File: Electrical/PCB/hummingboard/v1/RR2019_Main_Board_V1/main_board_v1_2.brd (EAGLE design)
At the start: 100 x 75 mm, 129 parts, among them CN1 MIRCO_B, J1 JTAG_SWD, J10 I2C_5V_4, J11 SERVO_LEFT, J12 SERVO_RIGHT, J13 ESC, J14 5V_INPUT, J15 QUAD_ENCODER_2, J17 I2C_5V_FXIO_1, J18 I2C_5V_FXIO_2, J2 REAR_ENCODER, J20 QUAD_ENCODER_1, J21 BLDC_HALL, J22 SPI_FXIO_1, J3 FRONT_ENCODER, J4 I2C_3V3_1, J5 SPI_2, J6 WIRELESS_MODULE, J7 UART_0, J8 UART_2, J9 STEERING_ANGLE, Q1 BSS138, Q2 BSS138, Q3 PMOS_SOT23, Q4 BSS138, Q5 BSS138, Q6 BSS138, Q7 BSS138, U1 MPU-9250(IMU)

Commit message: update on layout
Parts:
- added C23, L3, R42: TBD, RobotRacing2019_Master:0603SMT
- added J16: 7.2V_INPUT, RobotRacing2019_Master:JST_B2B-PH-K-S(LF)(SN)
- moved J13 12.7 mm to (29.4, 3.50)
- moved J12 6.95 mm to (17.9, 10.4)
- moved J11 6.93 mm to (29.4, 10.4)
- moved C6 4.89 mm to (14.1, 42.3)
- moved C18 2.91 mm to (41.9, 49.7)
- moved R21 2.82 mm to (43.2, 53.0)
- moved C11 2.80 mm to (30.8, 27.3)
- moved C12 2.80 mm to (35.7, 24.8)
- moved U1 2.80 mm to (30.8, 23.7)
- moved C10 2.71 mm to (35.9, 21.4)
- moved C3 1.70 mm to (27.6, 57.3), turned to 90 degrees
- moved C4 1.20 mm to (26.9, 32.9), turned to 270 degrees
- moved C1 1.08 mm to (30.8, 57.4), turned to 90 degrees
- moved JP12 0.90 mm to (-18.4, 14.1)
- moved C5 0.71 mm to (40.9, 44.4), turned to 0 degrees
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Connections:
- removed net PTA11: U$50.1
- new net +7.2V: C23.1, J11.1, J12.1, L3.2
- new net N$34: J16.1, R42.2
- new net N$36: L3.1, R42.1
- net +5V: no longer J11.1, J12.1
- net GND: now also C23.2, J16.2
- net PTA11_/_FTM1_CH5: now also U$50.1
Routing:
- net N$31: track 12.9 -> 99.2 mm, vias 0 -> 3
- net +5V: track 128.6 -> 42.5 mm
- net UART1_RTS: track 0.00 -> 75.1 mm, vias 0 -> 2
- net N$4: track 13.0 -> 84.0 mm, vias 0 -> 3
- net UART1_TX: track 0.00 -> 69.3 mm, vias 0 -> 2
- net UART1_RX: track 0.00 -> 68.6 mm, vias 0 -> 2
- net UART1_CTS: track 0.00 -> 68.1 mm, vias 0 -> 2
- net JTAG_TRST_B: track 7.21 -> 63.0 mm, vias 0 -> 2
- net SPI0_PCS3: track 0.00 -> 54.0 mm, vias 0 -> 2
- net SPI0_MOSI: track 3.21 -> 55.4 mm, vias 0 -> 2
- net SPI0_MISO: track 3.11 -> 55.1 mm, vias 0 -> 3
- net ADC0_SE10_/_ACMP0_IN5: track 0.00 -> 51.8 mm, vias 0 -> 2
- net N$41: track 9.43 -> 61.2 mm, vias 0 -> 2
- net FTM2_QD_PHA_/_TCLK2: track 0.00 -> 47.3 mm, vias 0 -> 1
- net SPI0_SCK: track 3.11 -> 49.8 mm, vias 0 -> 2
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
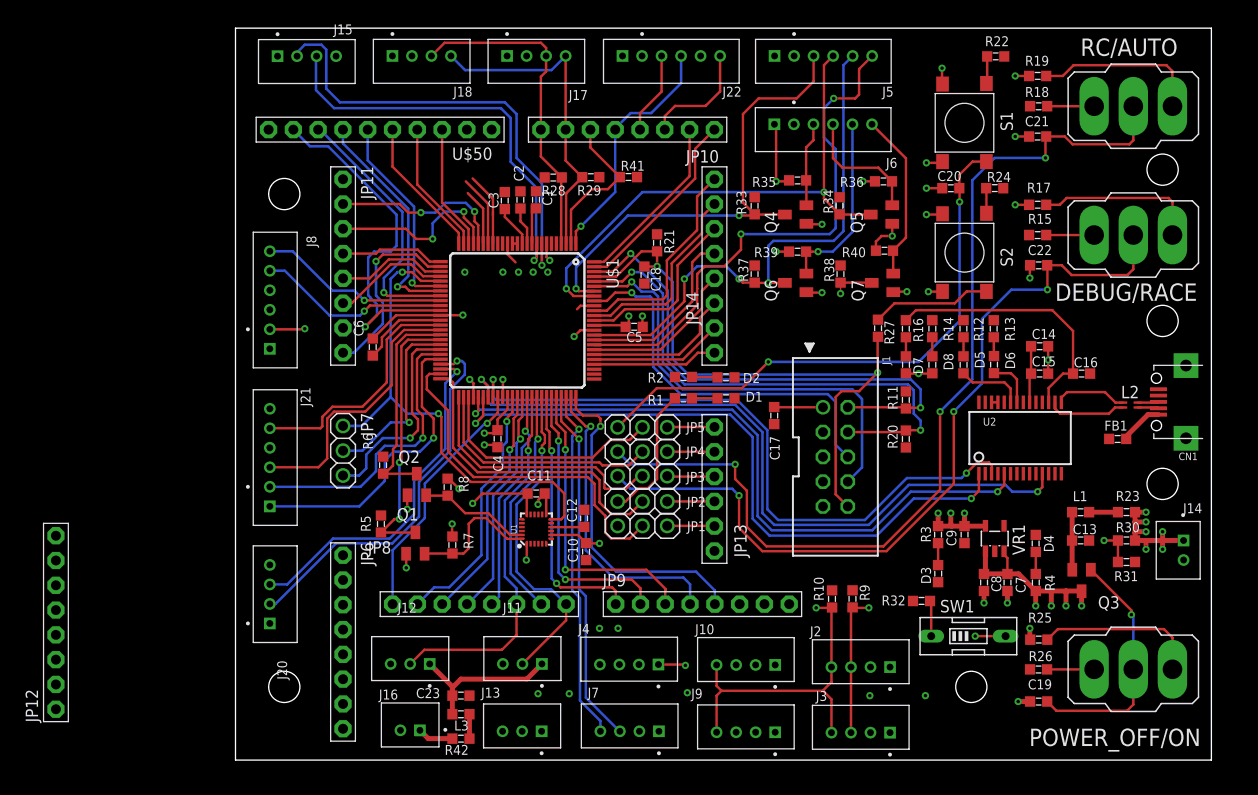
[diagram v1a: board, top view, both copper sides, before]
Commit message: simulation file added
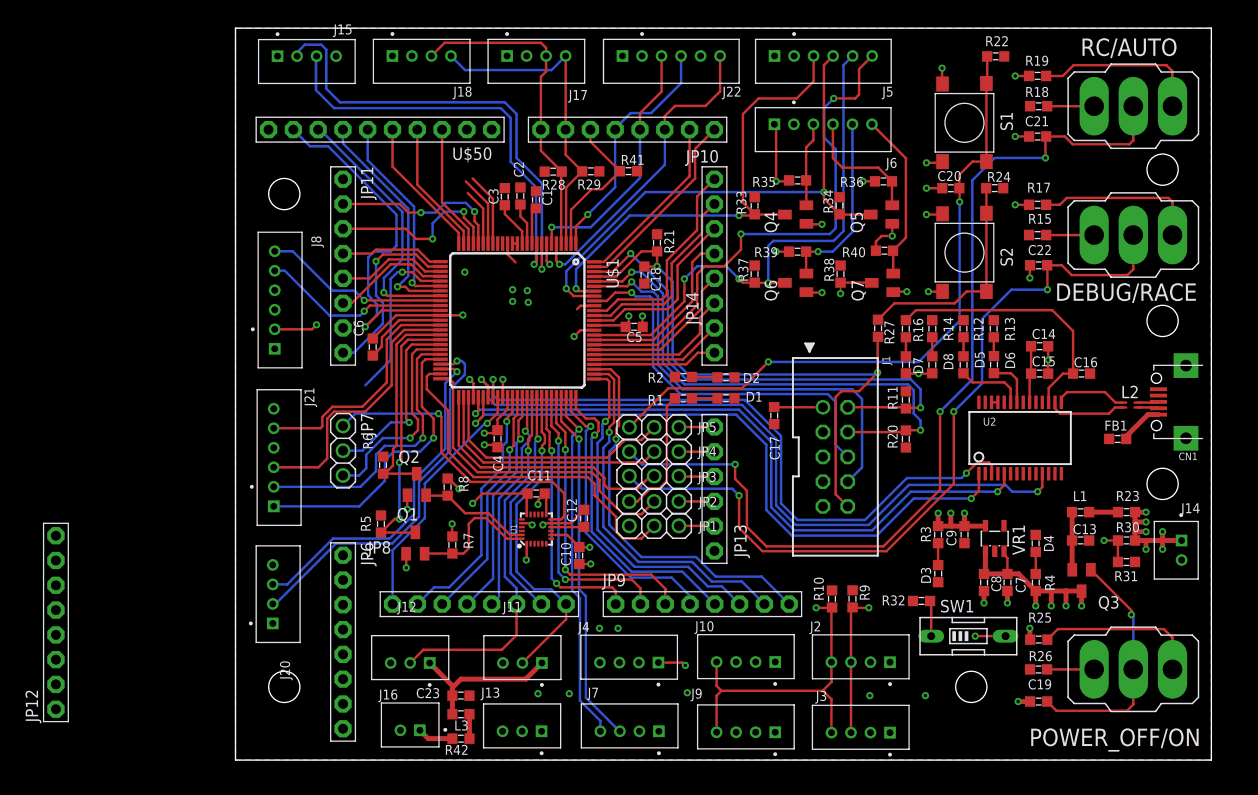
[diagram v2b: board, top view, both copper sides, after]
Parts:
- moved JP1 1.20 mm to (42.9, 24.0)
- moved JP2 1.20 mm to (42.9, 26.5)
- moved JP3 1.20 mm to (42.9, 29.1)
- moved JP4 1.20 mm to (42.9, 31.6)
- moved JP5 1.20 mm to (42.9, 34.1)
- moved C10 0.81 mm to (35.2, 21.0)
- moved R29 0.60 mm to (36.4, 60.3)
- moved R41 0.60 mm to (40.3, 60.3)
- moved R28 0.60 mm to (32.6, 60.3)
- moved J2 0.50 mm to (64.1, 10.6)
- moved J8 0.50 mm to (4.57, 47.1)
- moved J21 0.40 mm to (4.47, 31.0)
- moved C2 0.40 mm to (29.2, 57.8)
- moved C3 0.40 mm to (27.6, 57.7)
- moved J20 0.30 mm to (4.37, 17.0)
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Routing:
- net ADC0_SE1_/_ACMP0_IN1_/_FTM1_CH1: track 0.00 -> 40.2 mm, vias 0 -> 1
- net ADC2_SE11_/_FTM3_CH0: track 0.00 -> 37.6 mm, vias 0 -> 1
- net ADC2_SE10_/_FTM3_CH1: track 0.00 -> 35.1 mm, vias 0 -> 1
- net PWT_IN1_/_FXIO_D5: track 11.7 -> 32.6 mm, vias 0 -> 1
- net FTM2_CH4_/_FXIO_D4_/_TRGMUX_OUT4: track 8.47 -> 26.2 mm, vias 0 -> 1
- net GND: track 54.3 -> 62.3 mm, vias 27 -> 30
- net N$19: track 14.9 -> 22.9 mm
- net N$41: track 61.2 -> 68.0 mm
- net ADC2_SE9_/_FTM3_CH2: track 33.5 -> 31.2 mm
- net ADC2_SE8_/_FTM3_CH3: track 31.2 -> 29.4 mm
- net ADC0_SE10_/_ACMP0_IN5: track 51.8 -> 50.3 mm
- net N$31: track 99.2 -> 98.0 mm
- net ADC0_SE5_/_PTB1: track 24.2 -> 25.4 mm
- net DIGITAL_THREE: track 4.86 -> 3.66 mm
- net DIGITAL_TWO: track 4.84 -> 3.64 mm
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- added copper zone on layer 1, net GND

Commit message: [Journey Begins From Here] + new simulations and PCBs
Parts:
- removed J1: JTAG_SWD, RobotRacing2019_Master:CORTEXM3_SWD10_MOLEX
- removed JP12: POWER_2, adafruit:1X08-BIG
- removed POWER_OFF/ON: (no value), switch:320-916
- added C24: 0.1u, RobotRacing2019_Master:0603SMT
- added IC1: OR_SC70-5, RobotRacing2019_Master:SC70-5
- added J19: JETSON_TRIGGER, RobotRacing2019_Master:JST_B2B-PH-K-S(LF)(SN)
- added OFF/ON: (no value), switch:320-916
- added Q8: BSS138, RobotRacing2019_Master:SOT23
- added R43, R44: 10k, RobotRacing2019_Master:0603SMT
- added U$44: TEAM_LOGO, RobotRacing2019_Master:TEAM_LOGO
- Q3: value PMOS_SOT23 -> DMP2066LSN
- U$12: value TEAM_LOGO -> SWD_1.27MM; device RobotRacing2019_Master:TEAM_LOGO -> RobotRacing2019_Master:SWD_1.27MM
- moved U$12 34.8 mm to (61.3, 33.0), flipped to the top, turned to 270 degrees
- moved SW1 16.4 mm to (61.4, 21.8)
- moved J11 7.10 mm to (29.4, 3.40)
- moved J13 7.00 mm to (29.3, 10.5)
- moved R25 5.10 mm to (82.5, 7.24)
- moved C18 4.83 mm to (43.9, 54.1), turned to 90 degrees
- moved R26 4.70 mm to (82.3, 4.59)
- moved C19 3.70 mm to (82.3, 2.30)
- moved U$38 2.80 mm to (90.7, 0.80)
- moved R21 1.86 mm to (41.7, 54.1)
- moved Q3 1.25 mm to (85.6, 19.0)
- moved C13 1.25 mm to (85.5, 23.1)
- moved L1 1.25 mm to (85.5, 26.0)
- moved J14 0.50 mm to (96.1, 21.9)
- moved R23 0.50 mm to (91.0, 25.8)
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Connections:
- removed net 3V3: JP12.4, JP12.5, JP6.4, JP6.5
- removed net N$16: CN1.4
- removed net VDD: C1.1, C2.1, C3.1, C4.1, C5.1, C6.1, J15.1, J17.1, J18.1, J20.1, J22.1, J5.1, JP12.1, JP12.2, JP12.3, JP6.1, JP6.2, JP6.3, R10.2, R11.2, R15.2, R18.2, R21.2, R22.2, R24.2, R26.2, R28.2, R29.2, R41.2, R9.2, U$1.10, U$1.11, U$1.12, U$1.38, U$1.61, U$1.87
- new net N$35: J19.1, Q8.1
- new net N$38: IC1.2, Q8.3, R44.1
- new net N$39: IC1.4, Q3.1, R43.1
- net +3V3: now also JP6.4, JP6.5
- net +VDD: now also C1.1, C2.1, C24.2, C3.1, C4.1, C5.1, C6.1, IC1.5, J15.1, J17.1, J18.1, J20.1, J22.1, J5.1, JP6.1, JP6.2, JP6.3, R10.2, R11.2, R15.2, R18.2, R21.2, R22.2, R24.2, R26.2, R28.2, R29.2, R41.2, R43.2, R44.2, R9.2, U$1.10, U$1.11, U$1.12, U$1.38, U$1.61, U$1.87, U$12.1; no longer J1.1
- net GND: now also C24.1, IC1.3, Q8.2, U$12.3, U$12.5, U$12.7, U$12.9; no longer J1.3, J1.5, J1.7, J1.9, JP12.6, JP12.7, JP12.8
- net JTAG_TCLK/SWD_CLK: now also U$12.4; no longer J1.4
- net JTAG_TDI: now also U$12.8; no longer J1.8
- net JTAG_TDO/SWO: now also U$12.6; no longer J1.6
- net JTAG_TMS/SWD_DIO: now also U$12.2; no longer J1.2
- net JTAG_TRST_B: now also U$12.10; no longer J1.10
- net N$45: now also OFF/ON.3; no longer POWER_OFF/ON.3
- net N$46: now also OFF/ON.1; no longer POWER_OFF/ON.1
- net POWER_SHUT_DOWN: now also IC1.1, OFF/ON.2; no longer POWER_OFF/ON.2, Q3.1
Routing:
- net I2C0_SCL: track 16.9 -> 106.1 mm, vias 1 -> 3
- net I2C0_SDA: track 33.2 -> 98.1 mm, vias 1 -> 3
- net GND: track 62.3 -> 115.5 mm, vias 30 -> 38
- net SPI0_PCS0: track 6.32 -> 48.9 mm, vias 2 -> 3
- net ADC0_SE1_/_ACMP0_IN1_/_FTM1_CH1: track 40.2 -> 79.2 mm, vias 1 -> 3
- net VDD: track 32.2 -> 0.00 mm, vias 2 -> 0
- net +VDD: track 26.8 -> 56.7 mm, vias 4 -> 8
- net N$22: track 3.65 -> 31.6 mm, vias 0 -> 1
- net PTA11_/_FTM1_CH5: track 1.90 -> 26.9 mm, vias 0 -> 2
- net ACMP2_IN3_/_FTM0_FLT1: track 0.00 -> 21.7 mm
- net PTE13_/_FTM2_FLT0: track 2.26 -> 23.0 mm
- net N$6: track 0.00 -> 18.6 mm, vias 0 -> 1
- net N$38: track 0.00 -> 16.2 mm
- net UART2_RX: track 5.83 -> 22.0 mm, vias 0 -> 1
- net UART2_TX: track 7.32 -> 23.3 mm, vias 0 -> 1
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- added copper zone on layer 1, net +VDD
- removed copper zone on layer 15, net +3V3
- removed copper zone on layer 1, net GND
